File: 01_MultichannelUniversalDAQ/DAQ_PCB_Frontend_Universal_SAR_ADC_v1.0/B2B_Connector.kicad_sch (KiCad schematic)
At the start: 34 parts, among them U1 24AA02E

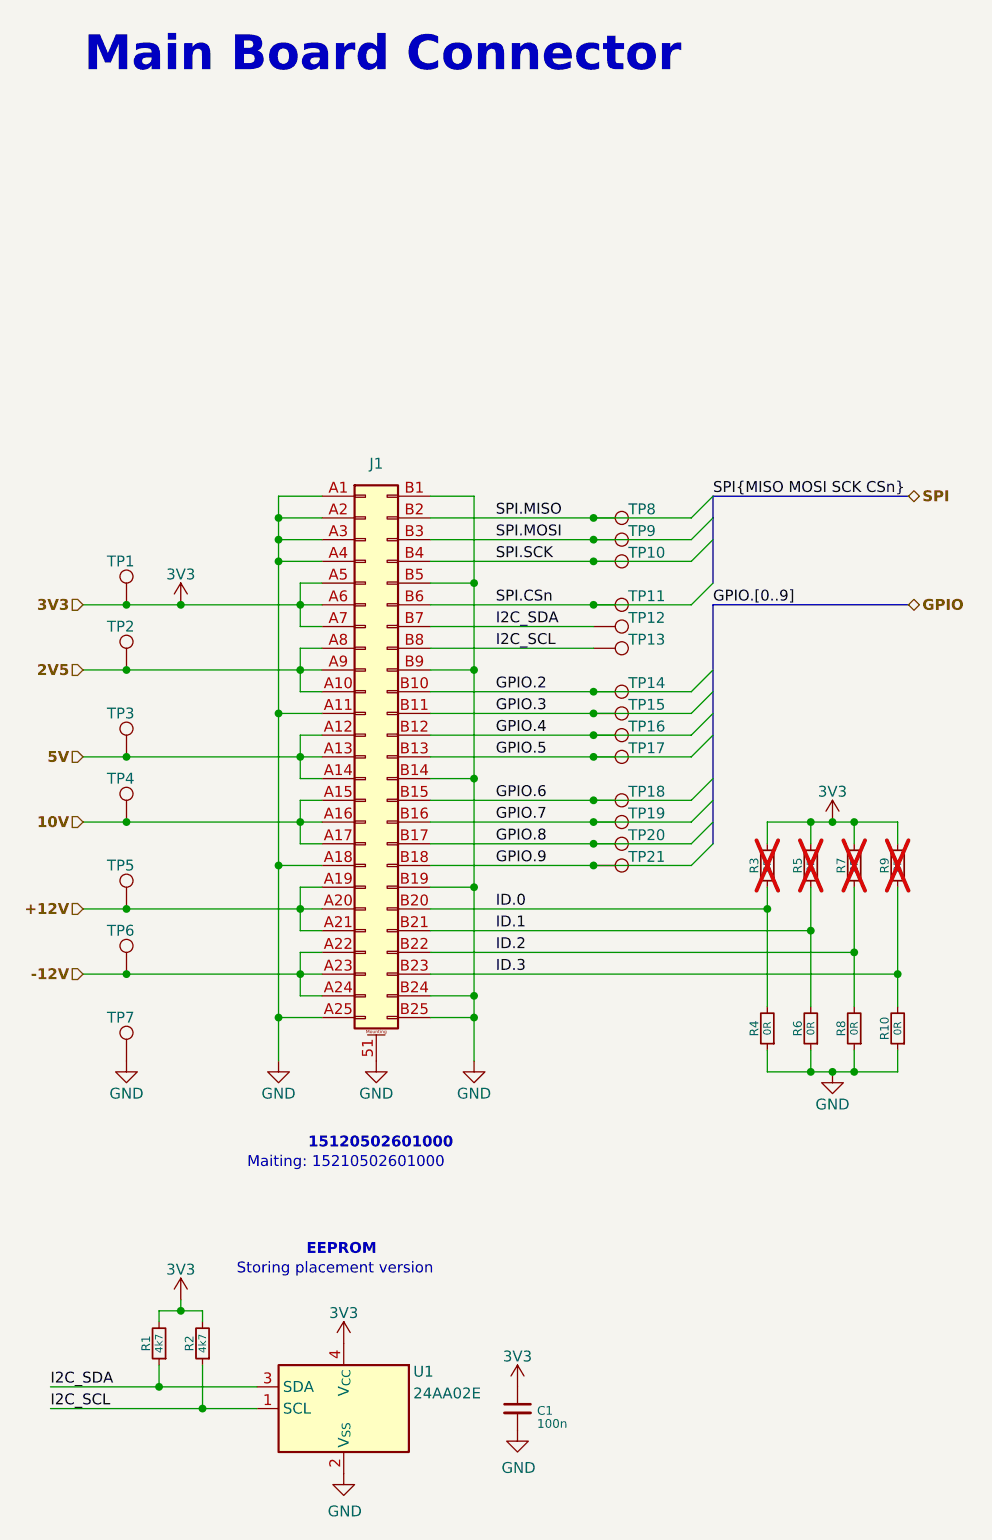
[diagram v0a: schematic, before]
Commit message: ADC és preamp in progress
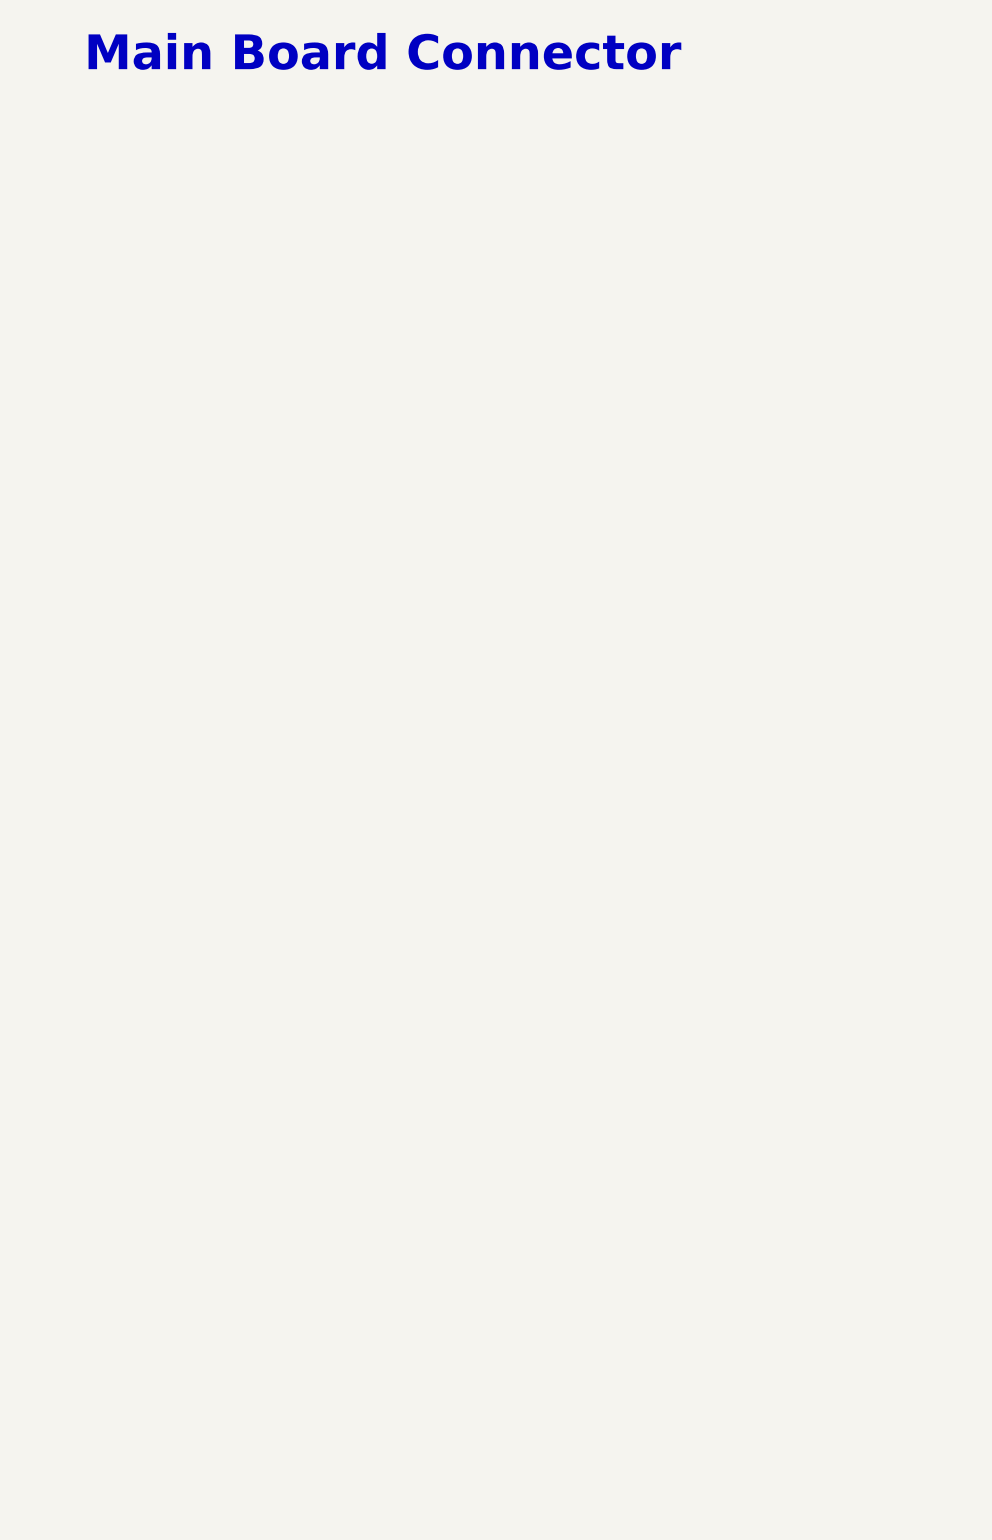
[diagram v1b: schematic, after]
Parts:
- removed C1: 100n, Capacitor_SMD:C_0603_1608Metric_Pad1.08x0.95mm_HandSolder, symbol Device:C_Small
- removed J1: (no value), KJ_KiCadLib_Others_Footprint:15120502601000, symbol KJ_KiCadLib:CONN_02x25_Hartning_B2B
- removed R1, R2: 4k7, Resistor_SMD:R_0603_1608Metric_Pad0.98x0.95mm_HandSolder, symbol Device:R_Small
- removed R10, R3, R4, R5, R6, R7, R8, R9: 0R, Resistor_SMD:R_0603_1608Metric_Pad0.98x0.95mm_HandSolder, symbol Device:R_Small
- removed TP1, TP10, TP11, TP12, TP13, TP14, TP15, TP16, TP17, TP18, TP19, TP2, TP20, TP21, TP3, TP4, TP5, TP6, TP7, TP8, TP9: TestPoint, TestPoint:TestPoint_Pad_D1.0mm, symbol Connector:TestPoint
- removed U1: 24AA02E, Package_TO_SOT_SMD:SOT-23-5, symbol Memory_EEPROM:24AA02E-OT
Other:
- note removed: "15120502601000"
- note removed: "EEPROM"
- note removed: "Maiting: 15210502601000"
- note removed: "Storing placement version"
